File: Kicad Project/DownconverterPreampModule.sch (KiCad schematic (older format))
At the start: 16 parts, among them U1 GALI-1+, U2 MCA1-85L+, U3 LMV751, U4 LMV751, U5 LMV751

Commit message: PCB Changes
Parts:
- U1: footprint (none) -> RadarComponents:Amplifier
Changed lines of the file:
@@
 F 0 "U1" H 2650 4350 60  0000 C CNN
 F 1 "GALI-1+" H 1950 4350 60  0000 C CNN
-F 2 "" H 2250 3800 60  0001 C CNN
+F 2 "RadarComponents:Amplifier" H 2250 3800 60  0001 C CNN
 F 3 "" H 2250 3800 60  0001 C CNN
 	1    2250 3800

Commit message: PCB and Schematic updates
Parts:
- C1, C2, C3, C4: footprint Capacitors_SMD:C_0603 -> RadarComponents:100PAD
- R1, R2: footprint Resistors_SMD:R_0603 -> RadarComponents:100PAD
- U2: footprint (none) -> RadarComponents:DZ885
- U3, U4, U5: footprint (none) -> RadarComponents:SOT23-5
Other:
- moved on the sheet: R1
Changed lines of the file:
@@
 F 0 "C1" H 1425 3900 50  0000 L CNN
 F 1 "270pF" H 1425 3700 50  0000 L CNN
-F 2 "Capacitors_SMD:C_0603" H 1438 3650 50  0001 C CNN
+F 2 "RadarComponents:100PAD" H 1438 3650 50  0001 C CNN
 F 3 "" H 1400 3800 50  0001 C CNN
 	1    1400 3800
@@
 $EndComp
 $Comp
-L GND #PWR015
+L GND #PWR019
 U 1 1 59FB8769
 P 2250 4250
-F 0 "#PWR015" H 2250 4000 50  0001 C CNN
+F 0 "#PWR019" H 2250 4000 50  0001 C CNN
 F 1 "GND" H 2250 4100 50  0000 C CNN
 F 2 "" H 2250 4250 50  0001 C CNN
@@
 F 0 "C3" H 3625 3900 50  0000 L CNN
 F 1 "270pF" H 3625 3700 50  0000 L CNN
-F 2 "Capacitors_SMD:C_0603" H 3638 3650 50  0001 C CNN
+F 2 "RadarComponents:100PAD" H 3638 3650 50  0001 C CNN
 F 3 "" H 3600 3800 50  0001 C CNN
 	1    3600 3800
@@
 F 0 "C2" H 3225 3400 50  0000 L CNN
 F 1 "270pF" H 3225 3200 50  0000 L CNN
-F 2 "Capacitors_SMD:C_0603" H 3238 3150 50  0001 C CNN
+F 2 "RadarComponents:100PAD" H 3238 3150 50  0001 C CNN
 F 3 "" H 3200 3300 50  0001 C CNN
 	1    3200 3300
@@
 L R R1
 U 1 1 59FB88C3
-P 2900 3550
-F 0 "R1" V 2980 3550 50  0000 C CNN
-F 1 "75" V 2900 3550 50  0000 C CNN
-F 2 "Resistors_SMD:R_0603" V 2830 3550 50  0001 C CNN
-F 3 "" H 2900 3550 50  0001 C CNN
-	1    2900 3550
+P 2950 3550
+F 0 "R1" V 3030 3550 50  0000 C CNN
+F 1 "75" V 2950 3550 50  0000 C CNN
+F 2 "RadarComponents:100PAD" V 2880 3550 50  0001 C CNN
+F 3 "" H 2950 3550 50  0001 C CNN
+	1    2950 3550
 	1    0    0    -1
 $EndComp
@@
 F 0 "R2" V 3330 2800 50  0000 C CNN
 F 1 "75" V 3250 2800 50  0000 C CNN
-F 2 "Resistors_SMD:R_0603" V 3180 2800 50  0001 C CNN
+F 2 "RadarComponents:100PAD" V 3180 2800 50  0001 C CNN
 F 3 "" H 3250 2800 50  0001 C CNN
 	1    3250 2800
 	0    1    1    0
 $EndComp
-Connection ~ 2900 3800
-Connection ~ 2900 3300
-$Comp
-L +9V #PWR016
+Connection ~ 2950 3800
+Connection ~ 2950 3300
+$Comp
+L +9V #PWR020
 U 1 1 59FB8AD6
 P 3600 2600
-F 0 "#PWR016" H 3600 2450 50  0001 C CNN
+F 0 "#PWR020" H 3600 2450 50  0001 C CNN
 F 1 "+9V" H 3600 2740 50  0000 C CNN
 F 2 "" H 3600 2600 50  0001 C CNN
@@
 $EndComp
 $Comp
-L GND #PWR017
+L GND #PWR021
 U 1 1 59FB8AF6
 P 3450 3400
-F 0 "#PWR017" H 3450 3150 50  0001 C CNN
+F 0 "#PWR021" H 3450 3150 50  0001 C CNN
 F 1 "GND" H 3450 3250 50  0000 C CNN
 F 2 "" H 3450 3400 50  0001 C CNN
@@
 	3450 3300 3450 3400
 Wire Wire Line
-	2900 3300 3050 3300
+	2950 3300 3050 3300
 $Comp
 L MCA1-85L+ U2
@@
 F 0 "U2" H 4300 4160 60  0000 C CNN
 F 1 "MCA1-85L+" H 4510 4270 60  0000 C CNN
-F 2 "" H 4850 3800 60  0001 C CNN
+F 2 "RadarComponents:DZ885" H 4850 3800 60  0001 C CNN
 F 3 "" H 4850 3800 60  0001 C CNN
 	1    4850 3800
@@
 	5450 5100 5450 3800
 $Comp
-L GND #PWR018
+L GND #PWR022
 U 1 1 59FB8C63
 P 4850 4400
-F 0 "#PWR018" H 4850 4150 50  0001 C CNN
+F 0 "#PWR022" H 4850 4150 50  0001 C CNN
 F 1 "GND" H 4850 4250 50  0000 C CNN
 F 2 "" H 4850 4400 50  0001 C CNN
@@
 F 0 "U3" H 6700 3050 60  0000 C CNN
 F 1 "LMV751" H 6100 3050 60  0000 C CNN
-F 2 "" H 6350 2500 60  0001 C CNN
+F 2 "RadarComponents:SOT23-5" H 6350 2500 60  0001 C CNN
 F 3 "" H 6350 2500 60  0001 C CNN
 	1    6350 2500
@@
 F 0 "C4" H 5575 3150 50  0000 L CNN
 F 1 "270pF" H 5575 2950 50  0000 L CNN
-F 2 "Capacitors_SMD:C_0603" H 5588 2900 50  0001 C CNN
+F 2 "RadarComponents:100PAD" H 5588 2900 50  0001 C CNN
 F 3 "" H 5550 3050 50  0001 C CNN
 	1    5550 3050
@@
 	5550 3200 5550 3300
 $Comp
-L GND #PWR019
+L GND #PWR023
 U 1 1 59FB902C
 P 5550 3300
-F 0 "#PWR019" H 5550 3050 50  0001 C CNN
+F 0 "#PWR023" H 5550 3050 50  0001 C CNN
 F 1 "GND" H 5550 3150 50  0000 C CNN
 F 2 "" H 5550 3300 50  0001 C CNN
@@
 	5650 2200 5750 2200
 $Comp
-L +9V #PWR020
+L +9V #PWR024
 U 1 1 59FB90DA
 P 7000 2150
-F 0 "#PWR020" H 7000 2000 50  0001 C CNN
+F 0 "#PWR024" H 7000 2000 50  0001 C CNN
 F 1 "+9V" H 7000 2290 50  0000 C CNN
 F 2 "" H 7000 2150 50  0001 C CNN
@@
 $EndComp
 $Comp
-L GND #PWR021
+L GND #PWR025
 U 1 1 59FB910C
 P 7000 2850
-F 0 "#PWR021" H 7000 2600 50  0001 C CNN
+F 0 "#PWR025" H 7000 2600 50  0001 C CNN
 F 1 "GND" H 7000 2700 50  0000 C CNN
 F 2 "" H 7000 2850 50  0001 C CNN
@@
 F 0 "U4" H 8600 3050 60  0000 C CNN
 F 1 "LMV751" H 8000 3050 60  0000 C CNN
-F 2 "" H 8250 2500 60  0001 C CNN
+F 2 "RadarComponents:SOT23-5" H 8250 2500 60  0001 C CNN
 F 3 "" H 8250 2500 60  0001 C CNN
 	1    8250 2500
@@
 Connection ~ 5650 2200
 $Comp
-L GND #PWR022
+L GND #PWR026
 U 1 1 59FB957B
 P 7650 2500
-F 0 "#PWR022" H 7650 2250 50  0001 C CNN
+F 0 "#PWR026" H 7650 2250 50  0001 C CNN
 F 1 "GND" H 7650 2350 50  0000 C CNN
 F 2 "" H 7650 2500 50  0001 C CNN
@@
 $EndComp
 $Comp
-L GND #PWR023
+L GND #PWR027
 U 1 1 59FB95A7
 P 8950 2900
-F 0 "#PWR023" H 8950 2650 50  0001 C CNN
+F 0 "#PWR027" H 8950 2650 50  0001 C CNN
 F 1 "GND" H 8950 2750 50  0000 C CNN
 F 2 "" H 8950 2900 50  0001 C CNN
@@
 $EndComp
 $Comp
-L +9V #PWR024
+L +9V #PWR028
 U 1 1 59FB95D3
 P 8950 2100
-F 0 "#PWR024" H 8950 1950 50  0001 C CNN
+F 0 "#PWR028" H 8950 1950 50  0001 C CNN
 F 1 "+9V" H 8950 2240 50  0000 C CNN
 F 2 "" H 8950 2100 50  0001 C CNN
@@
 F 0 "U5" H 10500 3050 60  0000 C CNN
 F 1 "LMV751" H 9900 3050 60  0000 C CNN
-F 2 "" H 10150 2500 60  0001 C CNN
+F 2 "RadarComponents:SOT23-5" H 10150 2500 60  0001 C CNN
 F 3 "" H 10150 2500 60  0001 C CNN
 	1    10150 2500
@@
 $EndComp
 $Comp
-L +9V #PWR025
+L +9V #PWR029
 U 1 1 59FB9877
 P 10850 2100
-F 0 "#PWR025" H 10850 1950 50  0001 C CNN
+F 0 "#PWR029" H 10850 1950 50  0001 C CNN
 F 1 "+9V" H 10850 2240 50  0000 C CNN
 F 2 "" H 10850 2100 50  0001 C CNN
@@
 $EndComp
 $Comp
-L GND #PWR026
+L GND #PWR030
 U 1 1 59FB98A7
 P 10850 2900
-F 0 "#PWR026" H 10850 2650 50  0001 C CNN
+F 0 "#PWR030" H 10850 2650 50  0001 C CNN
 F 1 "GND" H 10850 2750 50  0000 C CNN
 F 2 "" H 10850 2900 50  0001 C CNN
@@
 $EndComp
 $Comp
-L GND #PWR027
+L GND #PWR031
 U 1 1 59FB98E5
 P 9550 2500
-F 0 "#PWR027" H 9550 2250 50  0001 C CNN
+F 0 "#PWR031" H 9550 2250 50  0001 C CNN
 F 1 "GND" H 9550 2350 50  0000 C CNN
 F 2 "" H 9550 2500 50  0001 C CNN
@@
 OUTPUT
 Wire Wire Line
-	2900 3800 2900 3700
-Wire Wire Line
-	2900 2800 2900 3400
-Wire Wire Line
-	2900 2800 3100 2800
+	2950 3800 2950 3700
+Wire Wire Line
+	2950 2800 2950 3400
+Wire Wire Line
+	2950 2800 3100 2800
 Wire Wire Line
 	3400 2800 3600 2800

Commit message: fixed merge error
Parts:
- removed C4: 270pF, RadarComponents:100PAD, symbol C
- removed R3: 390k, Resistors_SMD:R_0603, symbol R
- removed U3: LMV751, RadarComponents:SOT23-5, symbol LMV751
- C1, C2, C3: footprint RadarComponents:100PAD -> Capacitors_SMD:C_0603
- R1, R2: footprint RadarComponents:100PAD -> Resistors_SMD:R_0603
- U1: symbol GALI-1+ -> GALI-1+-RESCUE-Radar
- U2: footprint RadarComponents:DZ885 -> (none)
- U4, U5: footprint RadarComponents:SOT23-5 -> (none)
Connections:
- wire segments 45 -> 33
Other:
- note added: "0.23737 inch single pole filter"
- moved on the sheet: R1
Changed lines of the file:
@@
 EESchema Schematic File Version 2
+LIBS:Radar-rescue
 LIBS:power
 LIBS:device
@@
 F 0 "C1" H 1425 3900 50  0000 L CNN
 F 1 "270pF" H 1425 3700 50  0000 L CNN
-F 2 "RadarComponents:100PAD" H 1438 3650 50  0001 C CNN
+F 2 "Capacitors_SMD:C_0603" H 1438 3650 50  0001 C CNN
 F 3 "" H 1400 3800 50  0001 C CNN
 	1    1400 3800
@@
 $EndComp
 $Comp
-L GALI-1+ U1
+L GALI-1+-RESCUE-Radar U1
 U 1 1 59FB86BB
 P 2250 3800
+AR Path="/59FB86BB" Ref="U1"  Part="1"
+AR Path="/59EFF5F0/59FB86BB" Ref="U1"  Part="1"
 F 0 "U1" H 2650 4350 60  0000 C CNN
 F 1 "GALI-1+" H 1950 4350 60  0000 C CNN
@@
 $EndComp
 $Comp
-L GND #PWR019
+L GND #PWR19
 U 1 1 59FB8769
 P 2250 4250
-F 0 "#PWR019" H 2250 4000 50  0001 C CNN
+F 0 "#PWR19" H 2250 4000 50  0001 C CNN
 F 1 "GND" H 2250 4100 50  0000 C CNN
 F 2 "" H 2250 4250 50  0001 C CNN
@@
 F 0 "C3" H 3625 3900 50  0000 L CNN
 F 1 "270pF" H 3625 3700 50  0000 L CNN
-F 2 "RadarComponents:100PAD" H 3638 3650 50  0001 C CNN
+F 2 "Capacitors_SMD:C_0603" H 3638 3650 50  0001 C CNN
 F 3 "" H 3600 3800 50  0001 C CNN
 	1    3600 3800
@@
 F 0 "C2" H 3225 3400 50  0000 L CNN
 F 1 "270pF" H 3225 3200 50  0000 L CNN
-F 2 "RadarComponents:100PAD" H 3238 3150 50  0001 C CNN
+F 2 "Capacitors_SMD:C_0603" H 3238 3150 50  0001 C CNN
 F 3 "" H 3200 3300 50  0001 C CNN
 	1    3200 3300
@@
 L R R1
 U 1 1 59FB88C3
-P 2950 3550
-F 0 "R1" V 3030 3550 50  0000 C CNN
-F 1 "75" V 2950 3550 50  0000 C CNN
-F 2 "RadarComponents:100PAD" V 2880 3550 50  0001 C CNN
-F 3 "" H 2950 3550 50  0001 C CNN
-	1    2950 3550
+P 2900 3550
+F 0 "R1" V 2980 3550 50  0000 C CNN
+F 1 "75" V 2900 3550 50  0000 C CNN
+F 2 "Resistors_SMD:R_0603" V 2830 3550 50  0001 C CNN
+F 3 "" H 2900 3550 50  0001 C CNN
+	1    2900 3550
 	1    0    0    -1
 $EndComp
@@
 F 0 "R2" V 3330 2800 50  0000 C CNN
 F 1 "75" V 3250 2800 50  0000 C CNN
-F 2 "RadarComponents:100PAD" V 3180 2800 50  0001 C CNN
+F 2 "Resistors_SMD:R_0603" V 3180 2800 50  0001 C CNN
 F 3 "" H 3250 2800 50  0001 C CNN
 	1    3250 2800
 	0    1    1    0
 $EndComp
-Connection ~ 2950 3800
-Connection ~ 2950 3300
-$Comp
-L +9V #PWR020
+Connection ~ 2900 3800
+Connection ~ 2900 3300
+$Comp
+L +9V #PWR21
 U 1 1 59FB8AD6
 P 3600 2600
-F 0 "#PWR020" H 3600 2450 50  0001 C CNN
+F 0 "#PWR21" H 3600 2450 50  0001 C CNN
 F 1 "+9V" H 3600 2740 50  0000 C CNN
 F 2 "" H 3600 2600 50  0001 C CNN
@@
 $EndComp
 $Comp
-L GND #PWR021
+L GND #PWR20
 U 1 1 59FB8AF6
 P 3450 3400
-F 0 "#PWR021" H 3450 3150 50  0001 C CNN
+F 0 "#PWR20" H 3450 3150 50  0001 C CNN
 F 1 "GND" H 3450 3250 50  0000 C CNN
 F 2 "" H 3450 3400 50  0001 C CNN
@@
 	3450 3300 3450 3400
 Wire Wire Line
-	2950 3300 3050 3300
+	2900 3300 3050 3300
 $Comp
 L MCA1-85L+ U2
@@
 F 0 "U2" H 4300 4160 60  0000 C CNN
 F 1 "MCA1-85L+" H 4510 4270 60  0000 C CNN
-F 2 "RadarComponents:DZ885" H 4850 3800 60  0001 C CNN
+F 2 "" H 4850 3800 60  0001 C CNN
 F 3 "" H 4850 3800 60  0001 C CNN
 	1    4850 3800
@@
 	5450 5100 5450 3800
 $Comp
-L GND #PWR022
+L GND #PWR22
 U 1 1 59FB8C63
 P 4850 4400
-F 0 "#PWR022" H 4850 4150 50  0001 C CNN
+F 0 "#PWR22" H 4850 4150 50  0001 C CNN
 F 1 "GND" H 4850 4250 50  0000 C CNN
 F 2 "" H 4850 4400 50  0001 C CNN
@@
 	1    0    0    -1
 $EndComp
-$Comp
-L LMV751 U3
-U 1 1 59FB8CCB
-P 6350 2500
-F 0 "U3" H 6700 3050 60  0000 C CNN
-F 1 "LMV751" H 6100 3050 60  0000 C CNN
-F 2 "RadarComponents:SOT23-5" H 6350 2500 60  0001 C CNN
-F 3 "" H 6350 2500 60  0001 C CNN
-	1    6350 2500
-	1    0    0    -1
-$EndComp
-$Comp
-L R R3
-U 1 1 59FB8E78
-P 5200 2800
-F 0 "R3" V 5280 2800 50  0000 C CNN
-F 1 "390k" V 5200 2800 50  0000 C CNN
-F 2 "Resistors_SMD:R_0603" V 5130 2800 50  0001 C CNN
-F 3 "" H 5200 2800 50  0001 C CNN
-	1    5200 2800
-	0    1    1    0
-$EndComp
-$Comp
-L C C4
-U 1 1 59FB8F1D
-P 5550 3050
-F 0 "C4" H 5575 3150 50  0000 L CNN
-F 1 "270pF" H 5575 2950 50  0000 L CNN
-F 2 "RadarComponents:100PAD" H 5588 2900 50  0001 C CNN
-F 3 "" H 5550 3050 50  0001 C CNN
-	1    5550 3050
-	1    0    0    -1
-$EndComp
-Wire Wire Line
-	4850 3200 4850 2800
-Wire Wire Line
-	4850 2800 5050 2800
-Wire Wire Line
-	5350 2800 5750 2800
-Wire Wire Line
-	5550 2900 5550 2800
-Connection ~ 5550 2800
-Wire Wire Line
-	5550 3200 5550 3300
-$Comp
-L GND #PWR023
-U 1 1 59FB902C
-P 5550 3300
-F 0 "#PWR023" H 5550 3050 50  0001 C CNN
-F 1 "GND" H 5550 3150 50  0000 C CNN
-F 2 "" H 5550 3300 50  0001 C CNN
-F 3 "" H 5550 3300 50  0001 C CNN
-	1    5550 3300
-	1    0    0    -1
-$EndComp
-Wire Wire Line
-	5650 2500 5750 2500
-Wire Wire Line
-	5650 1400 5650 2500
-Wire Wire Line
-	5650 2200 5750 2200
-$Comp
-L +9V #PWR024
-U 1 1 59FB90DA
-P 7000 2150
-F 0 "#PWR024" H 7000 2000 50  0001 C CNN
-F 1 "+9V" H 7000 2290 50  0000 C CNN
-F 2 "" H 7000 2150 50  0001 C CNN
-F 3 "" H 7000 2150 50  0001 C CNN
-	1    7000 2150
-	1    0    0    -1
-$EndComp
-$Comp
-L GND #PWR025
-U 1 1 59FB910C
-P 7000 2850
-F 0 "#PWR025" H 7000 2600 50  0001 C CNN
-F 1 "GND" H 7000 2700 50  0000 C CNN
-F 2 "" H 7000 2850 50  0001 C CNN
-F 3 "" H 7000 2850 50  0001 C CNN
-	1    7000 2850
-	1    0    0    -1
-$EndComp
-Wire Wire Line
-	6950 2200 7000 2200
-Wire Wire Line
-	7000 2200 7000 2150
-Wire Wire Line
-	6950 2800 7000 2800
-Wire Wire Line
-	7000 2800 7000 2850
-Text Notes 6000 3150 0    60   ~ 0
+Text Notes 5550 2950 0    60   ~ 0
 Low-Pass Filter
 $Comp
@@
 F 0 "U4" H 8600 3050 60  0000 C CNN
 F 1 "LMV751" H 8000 3050 60  0000 C CNN
-F 2 "RadarComponents:SOT23-5" H 8250 2500 60  0001 C CNN
+F 2 "" H 8250 2500 60  0001 C CNN
 F 3 "" H 8250 2500 60  0001 C CNN
 	1    8250 2500
@@
 	0    1    1    0
 $EndComp
-Wire Wire Line
-	5650 1400 7150 1400
-Wire Wire Line
-	7150 1400 7150 2800
-Connection ~ 5650 2200
-$Comp
-L GND #PWR026
+$Comp
+L GND #PWR23
 U 1 1 59FB957B
 P 7650 2500
-F 0 "#PWR026" H 7650 2250 50  0001 C CNN
+F 0 "#PWR23" H 7650 2250 50  0001 C CNN
 F 1 "GND" H 7650 2350 50  0000 C CNN
 F 2 "" H 7650 2500 50  0001 C CNN
@@
 $EndComp
 $Comp
-L GND #PWR027
+L GND #PWR25
 U 1 1 59FB95A7
 P 8950 2900
-F 0 "#PWR027" H 8950 2650 50  0001 C CNN
+F 0 "#PWR25" H 8950 2650 50  0001 C CNN
 F 1 "GND" H 8950 2750 50  0000 C CNN
 F 2 "" H 8950 2900 50  0001 C CNN
@@
 $EndComp
 $Comp
-L +9V #PWR028
+L +9V #PWR24
 U 1 1 59FB95D3
 P 8950 2100
-F 0 "#PWR028" H 8950 1950 50  0001 C CNN
+F 0 "#PWR24" H 8950 1950 50  0001 C CNN
 F 1 "+9V" H 8950 2240 50  0000 C CNN
 F 2 "" H 8950 2100 50  0001 C CNN
@@
 F 0 "U5" H 10500 3050 60  0000 C CNN
 F 1 "LMV751" H 9900 3050 60  0000 C CNN
-F 2 "RadarComponents:SOT23-5" H 10150 2500 60  0001 C CNN
+F 2 "" H 10150 2500 60  0001 C CNN
 F 3 "" H 10150 2500 60  0001 C CNN
 	1    10150 2500
@@
 $EndComp
 $Comp
-L +9V #PWR029
+L +9V #PWR27
 U 1 1 59FB9877
 P 10850 2100
-F 0 "#PWR029" H 10850 1950 50  0001 C CNN
+F 0 "#PWR27" H 10850 1950 50  0001 C CNN
 F 1 "+9V" H 10850 2240 50  0000 C CNN
 F 2 "" H 10850 2100 50  0001 C CNN
@@
 $EndComp
 $Comp
-L GND #PWR030
+L GND #PWR28
 U 1 1 59FB98A7
 P 10850 2900
-F 0 "#PWR030" H 10850 2650 50  0001 C CNN
+F 0 "#PWR28" H 10850 2650 50  0001 C CNN
 F 1 "GND" H 10850 2750 50  0000 C CNN
 F 2 "" H 10850 2900 50  0001 C CNN
@@
 $EndComp
 $Comp
-L GND #PWR031
+L GND #PWR26
 U 1 1 59FB98E5
 P 9550 2500
-F 0 "#PWR031" H 9550 2250 50  0001 C CNN
+F 0 "#PWR26" H 9550 2250 50  0001 C CNN
 F 1 "GND" H 9550 2350 50  0000 C CNN
 F 2 "" H 9550 2500 50  0001 C CNN
@@
 OUTPUT
 Wire Wire Line
-	2950 3800 2950 3700
-Wire Wire Line
-	2950 2800 2950 3400
-Wire Wire Line
-	2950 2800 3100 2800
+	2900 3800 2900 3700
+Wire Wire Line
+	2900 2800 2900 3400
+Wire Wire Line
+	2900 2800 3100 2800
 Wire Wire Line
 	3400 2800 3600 2800
+Wire Wire Line
+	4850 3200 4850 2800
+Wire Wire Line
+	4850 2800 7150 2800
+Text Notes 5200 3050 0    60   Italic 0
+0.23737 inch single pole filter
 $EndSCHEMATC

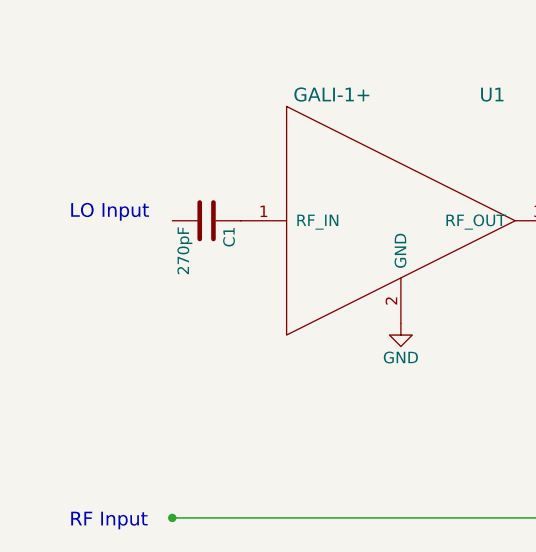
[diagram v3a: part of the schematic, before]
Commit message: PCB for source Module mostly complete, missing filter. Power Spliter still has issues.
Some minor changes made to all schematics for the net lists to be properall connected

A bunch of parts made
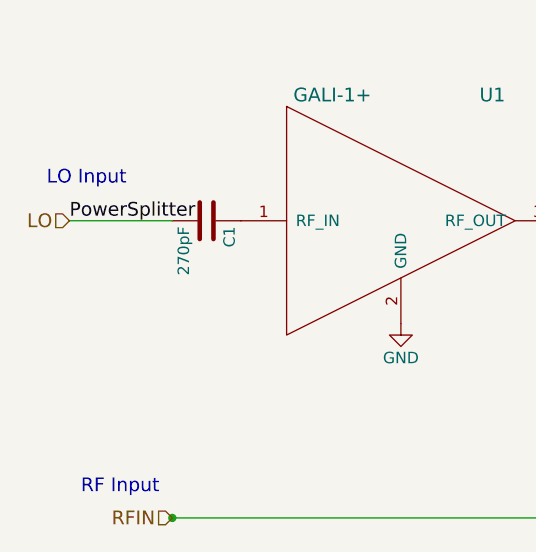
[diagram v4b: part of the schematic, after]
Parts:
- C1, C2, C3: footprint Capacitors_SMD:C_0603 -> RadarComponents:100PAD
- U2: footprint (none) -> RadarComponents:DZ885
- U4, U5: footprint (none) -> RadarComponents:SOT23-5
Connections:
- net LO: now reaches C1.2
- net RFIN: now reaches U2.5 (RF)
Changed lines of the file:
@@
 Comment4 ""
 $EndDescr
-Text Notes 800  3800 0    60   ~ 0
+Text Notes 700  3650 0    60   ~ 0
 LO Input
-Text Notes 800  5150 0    60   ~ 0
+Text Notes 850  5000 0    60   ~ 0
 RF Input
 $Comp
@@
 F 0 "C1" H 1425 3900 50  0000 L CNN
 F 1 "270pF" H 1425 3700 50  0000 L CNN
-F 2 "Capacitors_SMD:C_0603" H 1438 3650 50  0001 C CNN
+F 2 "RadarComponents:100PAD" H 1438 3650 50  0001 C CNN
 F 3 "" H 1400 3800 50  0001 C CNN
 	1    1400 3800
@@
 $EndComp
 $Comp
-L GND #PWR19
+L GND #PWR019
 U 1 1 59FB8769
 P 2250 4250
-F 0 "#PWR19" H 2250 4000 50  0001 C CNN
+F 0 "#PWR019" H 2250 4000 50  0001 C CNN
 F 1 "GND" H 2250 4100 50  0000 C CNN
 F 2 "" H 2250 4250 50  0001 C CNN
@@
 F 0 "C3" H 3625 3900 50  0000 L CNN
 F 1 "270pF" H 3625 3700 50  0000 L CNN
-F 2 "Capacitors_SMD:C_0603" H 3638 3650 50  0001 C CNN
+F 2 "RadarComponents:100PAD" H 3638 3650 50  0001 C CNN
 F 3 "" H 3600 3800 50  0001 C CNN
 	1    3600 3800
@@
 F 0 "C2" H 3225 3400 50  0000 L CNN
 F 1 "270pF" H 3225 3200 50  0000 L CNN
-F 2 "Capacitors_SMD:C_0603" H 3238 3150 50  0001 C CNN
+F 2 "RadarComponents:100PAD" H 3238 3150 50  0001 C CNN
 F 3 "" H 3200 3300 50  0001 C CNN
 	1    3200 3300
@@
 Connection ~ 2900 3300
 $Comp
-L +9V #PWR21
+L +9V #PWR020
 U 1 1 59FB8AD6
 P 3600 2600
-F 0 "#PWR21" H 3600 2450 50  0001 C CNN
+F 0 "#PWR020" H 3600 2450 50  0001 C CNN
 F 1 "+9V" H 3600 2740 50  0000 C CNN
 F 2 "" H 3600 2600 50  0001 C CNN
@@
 $EndComp
 $Comp
-L GND #PWR20
+L GND #PWR021
 U 1 1 59FB8AF6
 P 3450 3400
-F 0 "#PWR20" H 3450 3150 50  0001 C CNN
+F 0 "#PWR021" H 3450 3150 50  0001 C CNN
 F 1 "GND" H 3450 3250 50  0000 C CNN
 F 2 "" H 3450 3400 50  0001 C CNN
@@
 F 0 "U2" H 4300 4160 60  0000 C CNN
 F 1 "MCA1-85L+" H 4510 4270 60  0000 C CNN
-F 2 "" H 4850 3800 60  0001 C CNN
+F 2 "RadarComponents:DZ885" H 4850 3800 60  0001 C CNN
 F 3 "" H 4850 3800 60  0001 C CNN
 	1    4850 3800
@@
 	5450 5100 5450 3800
 $Comp
-L GND #PWR22
+L GND #PWR022
 U 1 1 59FB8C63
 P 4850 4400
-F 0 "#PWR22" H 4850 4150 50  0001 C CNN
+F 0 "#PWR022" H 4850 4150 50  0001 C CNN
 F 1 "GND" H 4850 4250 50  0000 C CNN
 F 2 "" H 4850 4400 50  0001 C CNN
@@
 F 0 "U4" H 8600 3050 60  0000 C CNN
 F 1 "LMV751" H 8000 3050 60  0000 C CNN
-F 2 "" H 8250 2500 60  0001 C CNN
+F 2 "RadarComponents:SOT23-5" H 8250 2500 60  0001 C CNN
 F 3 "" H 8250 2500 60  0001 C CNN
 	1    8250 2500
@@
 $EndComp
 $Comp
-L GND #PWR23
+L GND #PWR023
 U 1 1 59FB957B
 P 7650 2500
-F 0 "#PWR23" H 7650 2250 50  0001 C CNN
+F 0 "#PWR023" H 7650 2250 50  0001 C CNN
 F 1 "GND" H 7650 2350 50  0000 C CNN
 F 2 "" H 7650 2500 50  0001 C CNN
@@
 $EndComp
 $Comp
-L GND #PWR25
+L GND #PWR024
 U 1 1 59FB95A7
 P 8950 2900
-F 0 "#PWR25" H 8950 2650 50  0001 C CNN
+F 0 "#PWR024" H 8950 2650 50  0001 C CNN
 F 1 "GND" H 8950 2750 50  0000 C CNN
 F 2 "" H 8950 2900 50  0001 C CNN
@@
 $EndComp
 $Comp
-L +9V #PWR24
+L +9V #PWR025
 U 1 1 59FB95D3
 P 8950 2100
-F 0 "#PWR24" H 8950 1950 50  0001 C CNN
+F 0 "#PWR025" H 8950 1950 50  0001 C CNN
 F 1 "+9V" H 8950 2240 50  0000 C CNN
 F 2 "" H 8950 2100 50  0001 C CNN
@@
 F 0 "U5" H 10500 3050 60  0000 C CNN
 F 1 "LMV751" H 9900 3050 60  0000 C CNN
-F 2 "" H 10150 2500 60  0001 C CNN
+F 2 "RadarComponents:SOT23-5" H 10150 2500 60  0001 C CNN
 F 3 "" H 10150 2500 60  0001 C CNN
 	1    10150 2500
@@
 $EndComp
 $Comp
-L +9V #PWR27
+L +9V #PWR026
 U 1 1 59FB9877
 P 10850 2100
-F 0 "#PWR27" H 10850 1950 50  0001 C CNN
+F 0 "#PWR026" H 10850 1950 50  0001 C CNN
 F 1 "+9V" H 10850 2240 50  0000 C CNN
 F 2 "" H 10850 2100 50  0001 C CNN
@@
 $EndComp
 $Comp
-L GND #PWR28
+L GND #PWR027
 U 1 1 59FB98A7
 P 10850 2900
-F 0 "#PWR28" H 10850 2650 50  0001 C CNN
+F 0 "#PWR027" H 10850 2650 50  0001 C CNN
 F 1 "GND" H 10850 2750 50  0000 C CNN
 F 2 "" H 10850 2900 50  0001 C CNN
@@
 $EndComp
 $Comp
-L GND #PWR26
+L GND #PWR028
 U 1 1 59FB98E5
 P 9550 2500
-F 0 "#PWR26" H 9550 2250 50  0001 C CNN
+F 0 "#PWR028" H 9550 2250 50  0001 C CNN
 F 1 "GND" H 9550 2350 50  0000 C CNN
 F 2 "" H 9550 2500 50  0001 C CNN
@@
 Text Notes 5200 3050 0    60   Italic 0
 0.23737 inch single pole filter
+Text HLabel 800  3800 0    60   Input ~ 0
+LO
+Text HLabel 1250 5100 0    60   Input ~ 0
+RFIN
+Text Label 800  3800 0    60   ~ 0
+PowerSplitter
+Wire Wire Line
+	1250 3800 800  3800
 $EndSCHEMATC
